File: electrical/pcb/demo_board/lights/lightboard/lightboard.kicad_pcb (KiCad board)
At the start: 4 copper layers, 13 x 33.9 mm, 32 parts, among them J1 M20-9980346, J2 M20-9980346

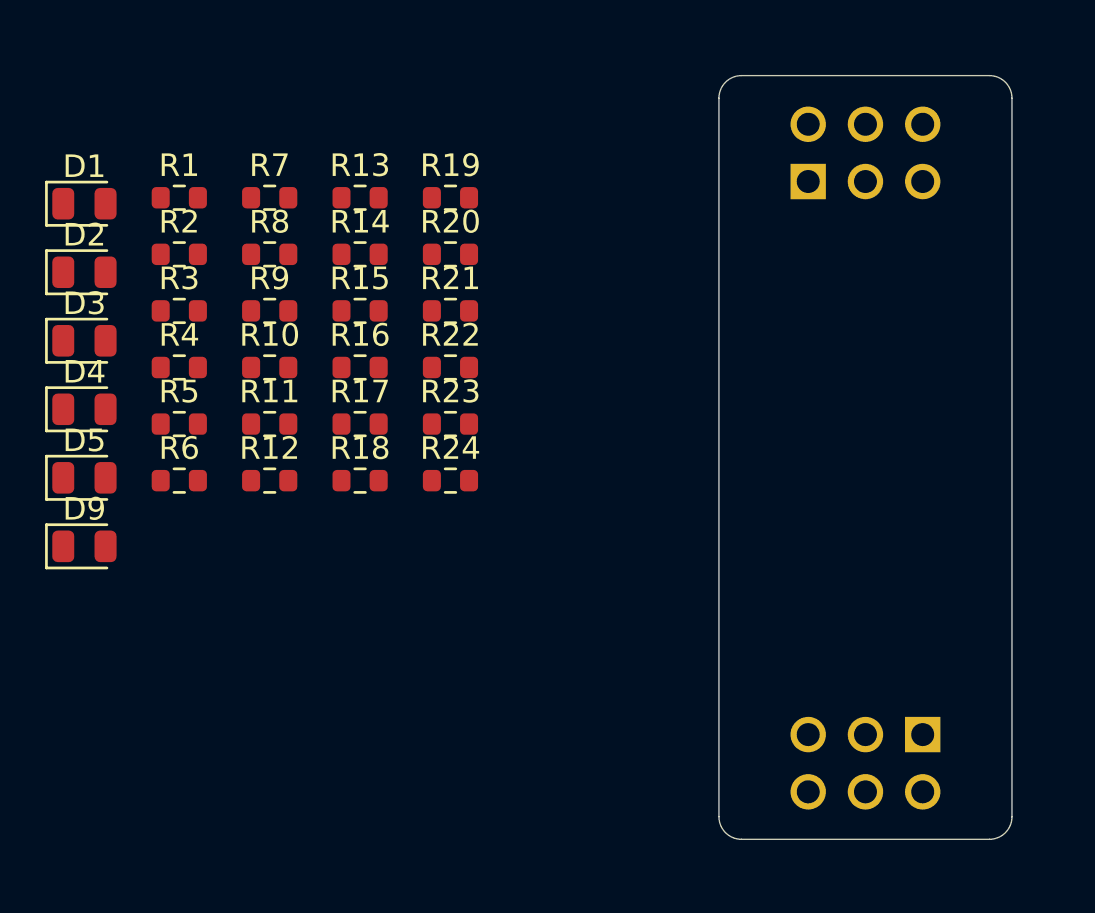
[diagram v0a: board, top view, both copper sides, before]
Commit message: ordered boards
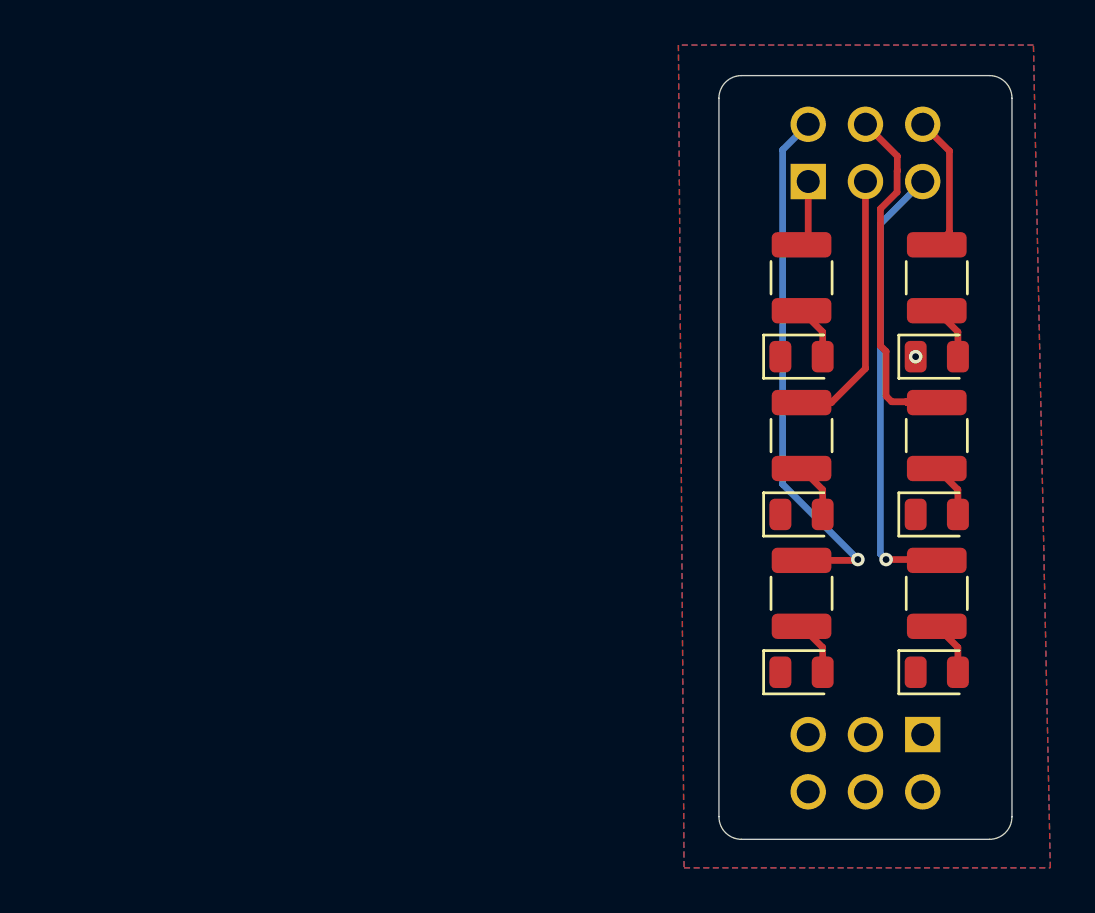
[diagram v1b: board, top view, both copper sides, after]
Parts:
- removed D9: LED, LED_SMD:LED_0805_2012Metric
- removed R10, R11, R12, R13, R14, R15, R16, R17, R18, R19, R20, R21, R22, R23, R24, R7, R8, R9: 33K, Resistor_SMD:R_0603_1608Metric
- added D6: LED, LED_SMD:LED_0805_2012Metric, F.Cu at (151.7, 114.5)
- R1, R2, R3, R4, R5, R6: footprint Resistor_SMD:R_0603_1608Metric -> Resistor_SMD:R_1210_3225Metric
- moved D1 38.4 mm to (151.7, 100.5)
- moved D4 38.1 mm to (151.7, 107.5)
- moved R6 34.0 mm to (151.7, 111.0), turned to -90 degrees
- moved R1 33.8 mm to (151.7, 97.0), turned to -90 degrees
- moved R4 33.7 mm to (151.7, 104.0), turned to -90 degrees
- moved D5 33.0 mm to (145.7, 114.5)
- moved D3 32.7 mm to (145.7, 107.5)
- moved D2 32.0 mm to (145.7, 100.5)
- moved R5 28.6 mm to (145.7, 111.0), turned to -90 degrees
- moved R3 28.2 mm to (145.7, 104.0), turned to -90 degrees
- moved R2 27.6 mm to (145.7, 97.0), turned to -90 degrees
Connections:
- J1 pad 1: (no net) -> /P2
- J1 pad 2: (no net) -> /P5
- J1 pad 3: (no net) -> /P3
- J1 pad 4: (no net) -> /P4
- J1 pad 5: (no net) -> /P6
- J1 pad 6: (no net) -> /P1
- J2 pad 1: (no net) -> GND
- J2 pad 2: (no net) -> GND
- J2 pad 3: (no net) -> GND
- J2 pad 4: (no net) -> GND
- J2 pad 5: (no net) -> GND
- J2 pad 6: (no net) -> GND
- R1 pad 1: unconnected-(R1-Pad1) -> /P1
- R1 pad 2: Net-(R1-Pad2) -> Net-(D1-A)
- R2 pad 1: Net-(R1-Pad2) -> /P2
- R2 pad 2: Net-(R2-Pad2) -> Net-(D2-A)
- R3 pad 1: Net-(R2-Pad2) -> /P3
- R3 pad 2: Net-(R3-Pad2) -> Net-(D3-A)
- R4 pad 1: Net-(R3-Pad2) -> /P4
- R4 pad 2: Net-(D9-A) -> Net-(D4-A)
- R5 pad 1: unconnected-(R5-Pad1) -> /P5
- R5 pad 2: Net-(R5-Pad2) -> Net-(D5-A)
- R6 pad 1: Net-(R5-Pad2) -> /P6
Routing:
- net /P5: track 0.00 -> 23.7 mm, vias 0 -> 1
- net /P6: track 0.00 -> 19.9 mm, vias 0 -> 1
- net /P4: track 0.00 -> 15.4 mm
- net /P3: track 0.00 -> 11.8 mm
- net /P1: track 0.00 -> 6.07 mm
- net /P2: track 0.00 -> 2.93 mm
- net Net-(D6-A): track 0.00 -> 2.43 mm
- net Net-(D5-A): track 0.00 -> 2.43 mm
- net Net-(D4-A): track 0.00 -> 2.43 mm
- net Net-(D3-A): track 0.00 -> 2.43 mm
- net Net-(D2-A): track 0.00 -> 2.43 mm
- net Net-(D1-A): track 0.00 -> 2.43 mm
- net GND: vias 0 -> 1
- added copper zone on B.Cu, net GND
- added copper zone on F.Cu, net GND
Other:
- copper layers 4 -> 2
